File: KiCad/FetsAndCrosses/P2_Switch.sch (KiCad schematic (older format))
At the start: 0 parts

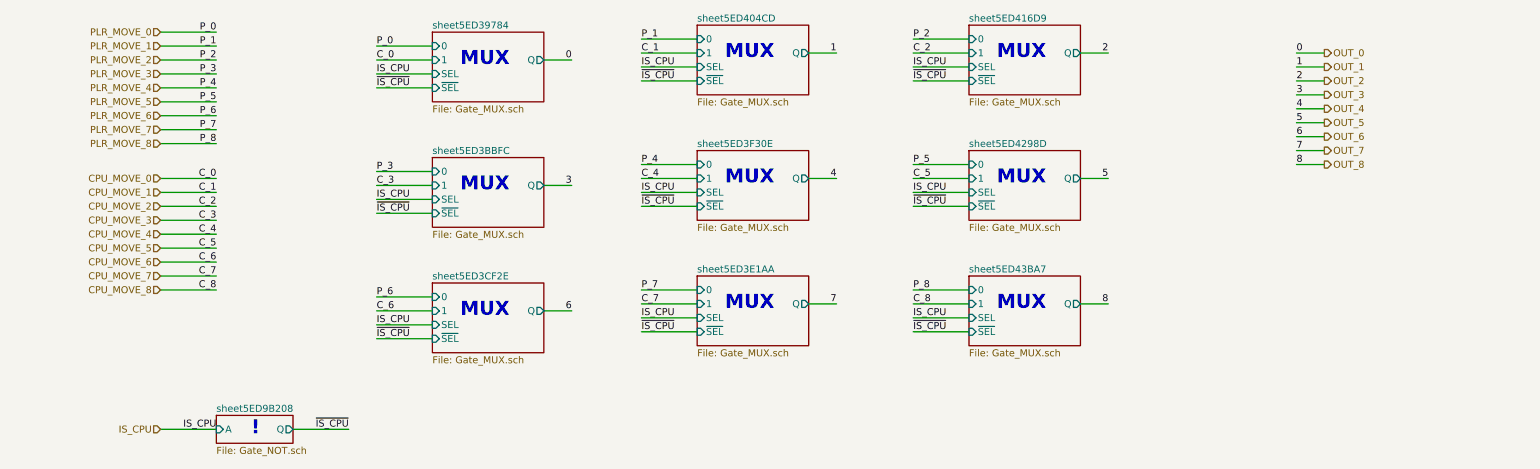
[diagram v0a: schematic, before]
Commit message: Reworked everything to use Buses
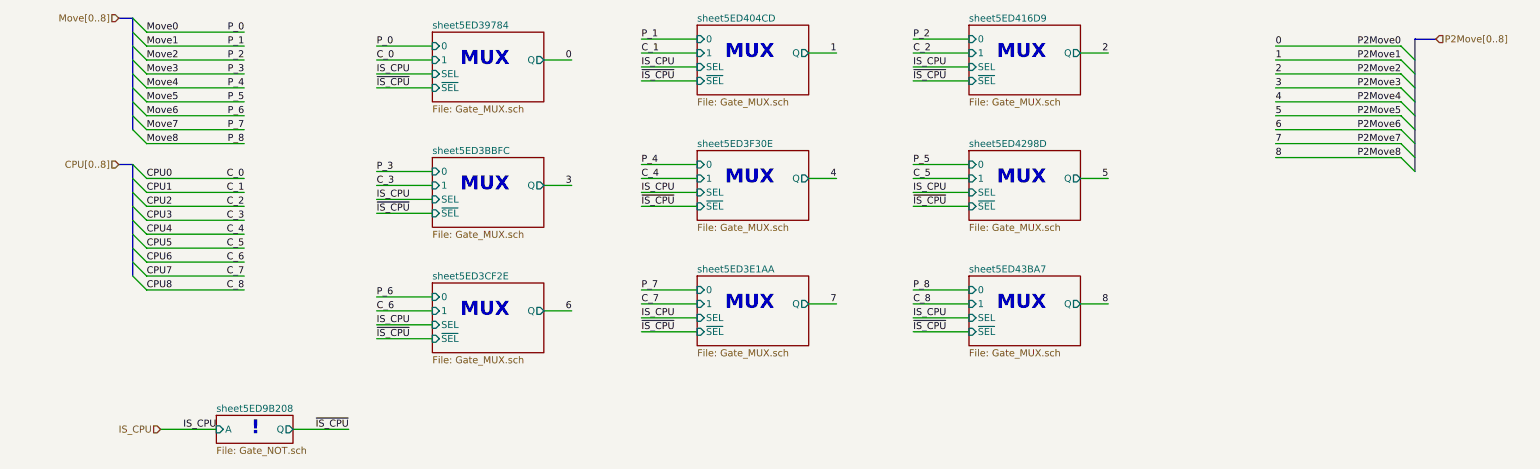
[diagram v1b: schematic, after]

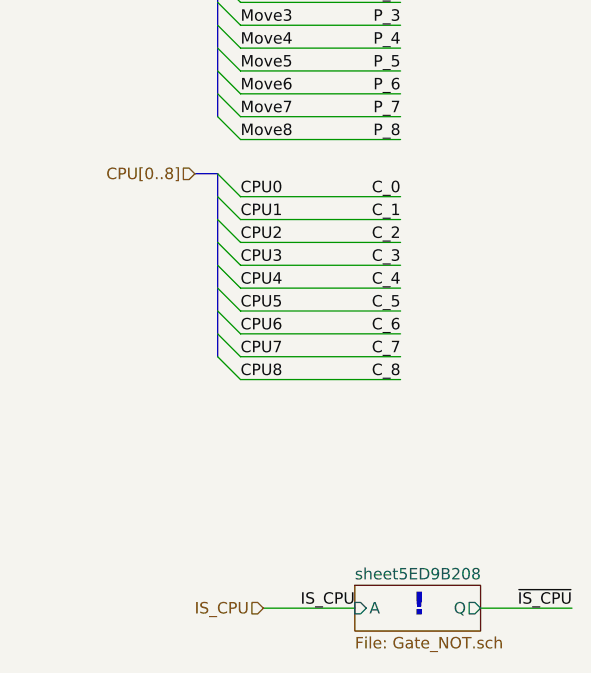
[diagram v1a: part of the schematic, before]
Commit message: Schematic Done, Footprints assigned, ERC OK.
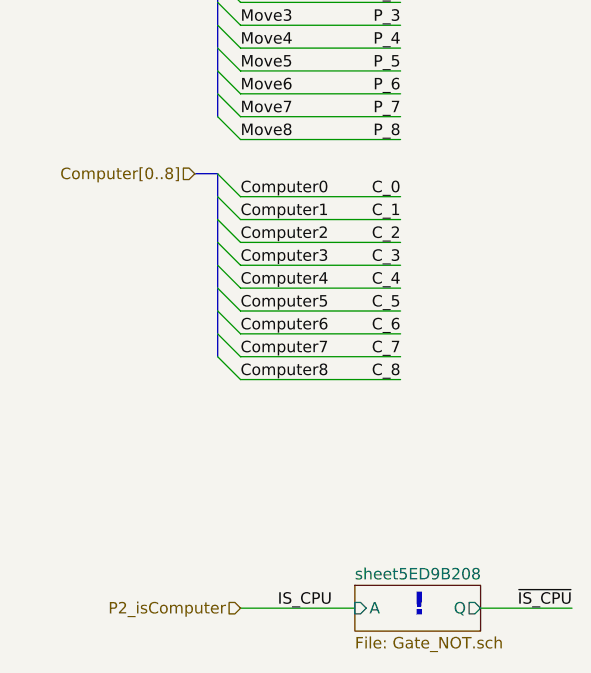
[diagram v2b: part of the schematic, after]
